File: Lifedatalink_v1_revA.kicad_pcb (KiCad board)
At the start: 4 copper layers, 69.5 x 72.5 mm, 88 parts, among them J1 DX07S024XJ1R1100, J10 503480-0400, J11 5034801400, J12 5034801400, J13 503480-0600, J14 503480-0600, J15 503480-0600, J16 503480-0600, J2 BATTERY CONNECTOR, J4 Conn_01x06, J5 503480-0400, J6 503480-0400, J7 503480-0400, J8 503480-0400, J9 503480-0400, Q1 DMG2301L, SW1 SW_Push, U1 BL654, U2 LP5907MFX-3_3_NOPB, U3 ADS1292R, U4 MCP73831-2-OT, U5 TMP117NAIYBGR, U6 MAX30102, U7 LP5907MFX-1.8, U8 IIS2DLPCTR, U9 PCA9306, Y1 Crystal

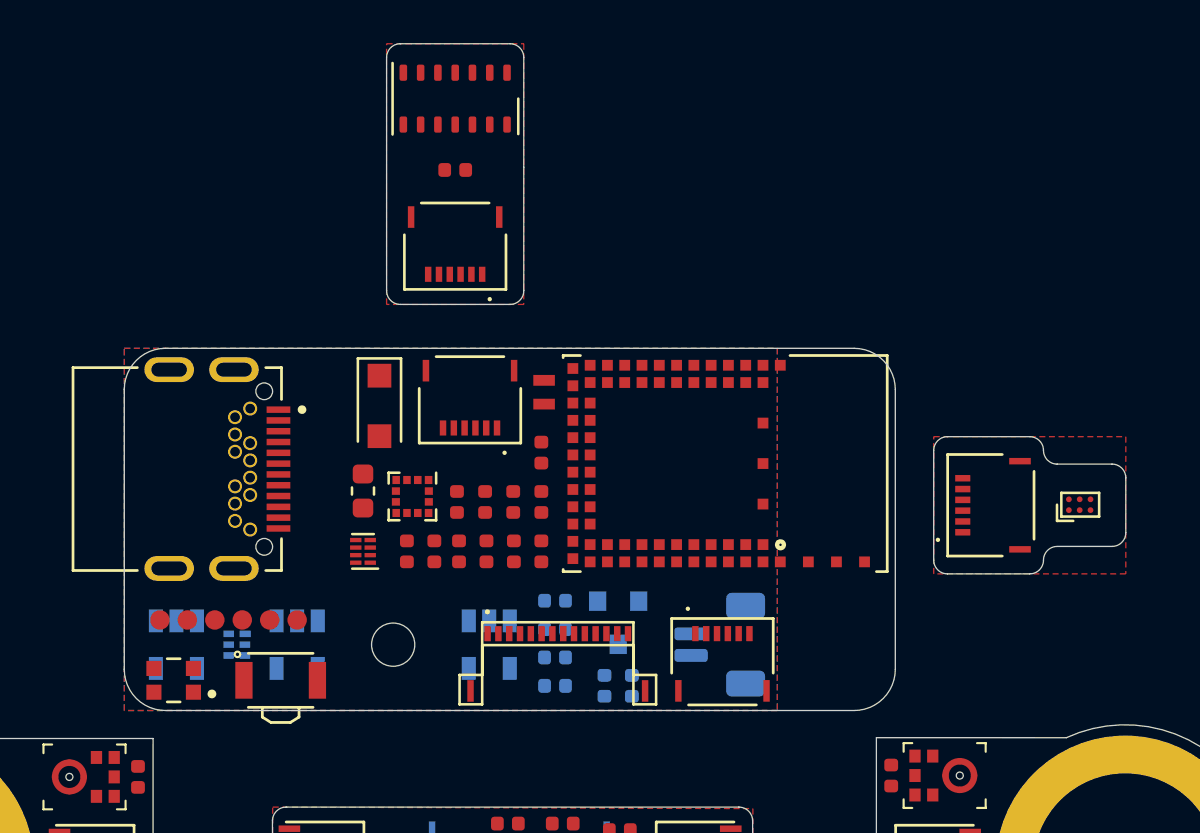
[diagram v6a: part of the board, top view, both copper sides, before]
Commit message: Main board routed
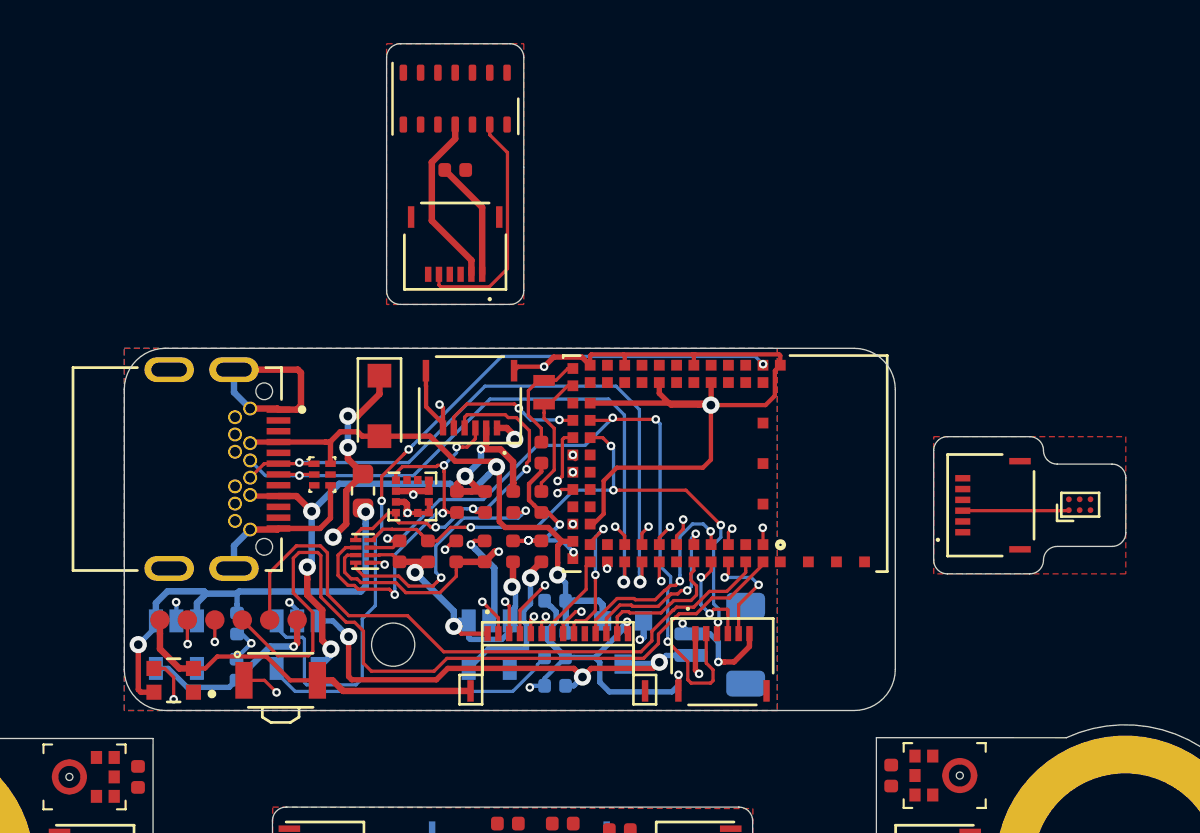
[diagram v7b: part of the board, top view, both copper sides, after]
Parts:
- D1: moved to F.Cu
- moved C3 18.5 mm to (73.1, 93.3)
- moved C4 14.9 mm to (73.1, 95.5), turned to 270 degrees
- moved D1 8.81 mm to (77.0, 86.4)
- moved R4 3.34 mm to (87.8, 93.8), turned to 0 degrees
- moved Q1 0.94 mm to (91.0, 94.2)
- moved R19 0.34 mm to (80.6, 90.0)
- moved R18 0.30 mm to (81.9, 90.0), turned to 90 degrees
- moved C28 0.13 mm to (83.2, 90.0)
- moved C27 0.09 mm to (84.5, 90.0)
- turned C25 to 270 degrees
- turned C26 to 270 degrees
- turned J4 to 180 degrees
- turned U8 to 0 degrees
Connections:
- C26 pad 1: Net-(C26-Pad1) -> GND
- C3 pad 2: Net-(C3-Pad2) -> /VIN
- D3 pad K: Net-(C3-Pad2) -> /VIN_FUSE
- F1 pad 1: Net-(F1-Pad1) -> /VIN
- F1 pad 2: Net-(C3-Pad2) -> /VIN_FUSE
- J11 pad 11: /BL654_I2S_WS -> /BL654_I2S_WS_EXT
- J11 pad 12: /BL654_I2S_SCK -> /BL654_I2S_SCK_EXT
- J11 pad 13: /BL654_I2S_SD -> /BL654_I2S_SD_EXT
- J11 pad 2: /ADS_SPI_SCLK -> /ADS_SPI_SCLK_EXT
- J11 pad 3: /ADS_SPI_MISO -> /ADS_SPI_MISO_EXT
- J11 pad 4: /ADS_SPI_MOSI -> /ADS_SPI_MOSI_EXT
- J11 pad 5: /~ADS_SPI_CS -> /~ADS_SPI_CS_EXT
- J11 pad 6: /~ADS_PWDN_RESET -> /~ADS_PWDN_RESET_EXT
- J11 pad 7: /ADS_START -> /ADS_START_EXT
- J11 pad 8: /ADS_CLK -> /ADS_CLK_EXT
- J11 pad 9: /~ADS_DRDY -> /~ADS_DRDY_EXT
- J13 pad 2: /BL654_I2C_SCL_HV -> /BL654_I2C_SCL_HV_EXT
- J13 pad 3: /BL654_I2C_SDA_HV -> /BL654_I2C_SDA_HV_EXT
- J13 pad 4: /TMP_ALERT -> /TMP_ALERT_EXT
- J13 pad 5: /TMP_ADD0 -> /TMP_ADD0_EXT
- J16 pad 3: /BL654_I2C_SCL_LV -> /BL654_I2C_SCL_LV_EXT
- J16 pad 4: /BL654_I2C_SDA_LV -> /BL654_I2C_SDA_LV_EXT
- J16 pad 5: /~MAX_INT -> /~MAX_INT_EXT
- J4 pad 1: Net-(J4-Pad1) -> +3V3
- MIC1 pad 1: /BL654_I2S_WS -> /BL654_I2S_WS_EXT
- MIC1 pad 4: /BL654_I2S_SCK -> /BL654_I2S_SCK_EXT
- MIC1 pad 6: /BL654_I2S_SD -> /BL654_I2S_SD_EXT
- MIC2 pad 1: /BL654_I2S_WS -> /BL654_I2S_WS_EXT
- MIC2 pad 4: /BL654_I2S_SCK -> /BL654_I2S_SCK_EXT
- MIC2 pad 6: /BL654_I2S_SD -> /BL654_I2S_SD_EXT
- Q1 pad 2: Net-(C3-Pad2) -> /VIN_FUSE
- R22 pad 1: /BL654_I2S_SD -> /BL654_I2S_SD_EXT
- U1 pad 12: Net-(U1-Pad12) -> /ADS_SPI_SCLK
- U1 pad 13: Net-(U1-Pad13) -> /ADS_SPI_MISO
- U1 pad 14: Net-(U1-Pad14) -> /ADS_SPI_MOSI
- U1 pad 16: Net-(U1-Pad16) -> /~ADS_PWDN_RESET
- U1 pad 18: Net-(U1-Pad18) -> /ADS_CLK
- U1 pad 19: Net-(U1-Pad19) -> /~ADS_SPI_CS
- U1 pad 21: Net-(U1-Pad21) -> /ADS_START
- U1 pad 22: Net-(U1-Pad22) -> /~ADS_DRDY
- U1 pad 30: /ADS_CLK -> Net-(U1-Pad30)
- U1 pad 32: /~ADS_DRDY -> Net-(U1-Pad32)
- U1 pad 37: Net-(U1-Pad37) -> /~MAX_INT
- U1 pad 44: /TMP_ADD0 -> Net-(U1-Pad44)
- U1 pad 5: Net-(U1-Pad5) -> /TMP_ADD0
- U1 pad 51: /ADS_SPI_MISO -> Net-(U1-Pad51)
- U1 pad 53: /ADS_SPI_SCLK -> Net-(U1-Pad53)
- U1 pad 54: /~ADS_SPI_CS -> Net-(U1-Pad54)
- U1 pad 56: /ADS_SPI_MOSI -> Net-(U1-Pad56)
- U1 pad 60: /~ADS_PWDN_RESET -> Net-(U1-Pad60)
- U1 pad 62: /ADS_START -> Net-(U1-Pad62)
- U2 pad 1: Net-(F1-Pad1) -> /VIN
- U2 pad 3: Net-(F1-Pad1) -> /VIN
- U3 pad 15: /~ADS_PWDN_RESET -> /~ADS_PWDN_RESET_EXT
- U3 pad 16: /ADS_START -> /ADS_START_EXT
- U3 pad 17: /ADS_CLK -> /ADS_CLK_EXT
- U3 pad 18: /~ADS_SPI_CS -> /~ADS_SPI_CS_EXT
- U3 pad 19: /ADS_SPI_MOSI -> /ADS_SPI_MOSI_EXT
- U3 pad 20: /ADS_SPI_SCLK -> /ADS_SPI_SCLK_EXT
- U3 pad 21: /ADS_SPI_MISO -> /ADS_SPI_MISO_EXT
- U3 pad 22: /~ADS_DRDY -> /~ADS_DRDY_EXT
- U5 pad A1: /BL654_I2C_SDA_HV -> /BL654_I2C_SDA_HV_EXT
- U5 pad A2: /BL654_I2C_SCL_HV -> /BL654_I2C_SCL_HV_EXT
- U5 pad C1: /TMP_ADD0 -> /TMP_ADD0_EXT
- U5 pad C2: /TMP_ALERT -> /TMP_ALERT_EXT
- U6 pad 13: /~MAX_INT -> /~MAX_INT_EXT
- U6 pad 2: /BL654_I2C_SCL_LV -> /BL654_I2C_SCL_LV_EXT
- U6 pad 3: /BL654_I2C_SDA_LV -> /BL654_I2C_SDA_LV_EXT
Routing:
- net GND: track 0.00 -> 121.3 mm, vias 0 -> 20
- net +3V3: track 0.00 -> 64.4 mm, vias 0 -> 8
- net +5V: track 0.00 -> 47.7 mm, vias 0 -> 5
- net +1V8: track 0.00 -> 45.7 mm, vias 0 -> 5
- net /WS2812_DATA: track 0.00 -> 38.5 mm, vias 0 -> 2
- net /BL654_SWDIO: track 0.00 -> 37.3 mm
- net /MCP73831_STAT: track 0.00 -> 36.5 mm, vias 0 -> 3
- net /BL654_I2C_SCL_HV: track 0.00 -> 34.3 mm, vias 0 -> 4
- net Net-(SW1-Pad1): track 0.00 -> 31.4 mm, vias 0 -> 2
- net /BL654_SWDCLK: track 0.00 -> 30.2 mm
- net /BL654_USB_DP: track 0.00 -> 29.9 mm, vias 0 -> 2
- net /BL654_USB_DN: track 0.00 -> 29.7 mm, vias 0 -> 2
- net /BL654_UART_RX: track 0.00 -> 28.5 mm, vias 0 -> 2
- net /BL654_UART_TX: track 0.00 -> 27.5 mm, vias 0 -> 2
- net /VIN_FUSE: track 0.00 -> 27.4 mm, vias 0 -> 4
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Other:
- net class Power: clearance 0.2 -> 0.1524

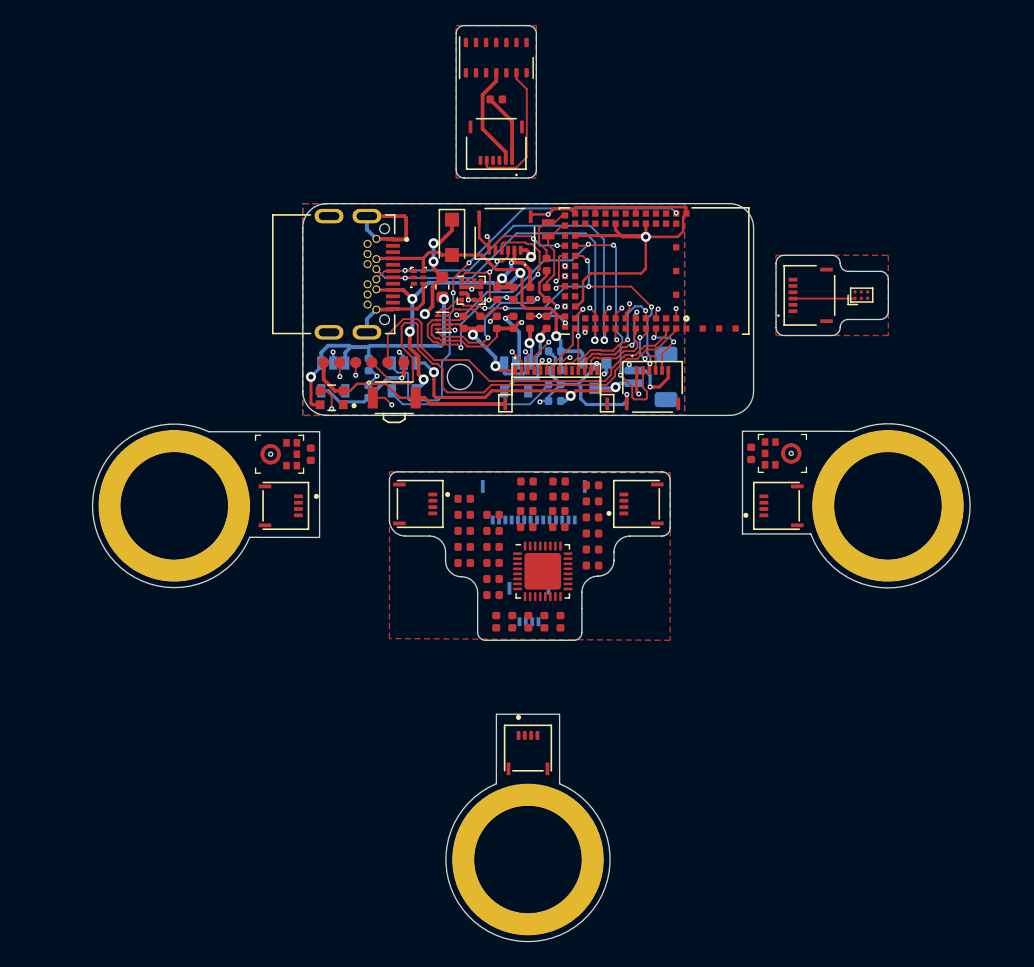
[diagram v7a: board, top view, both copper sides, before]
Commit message: Completed routing of all boards
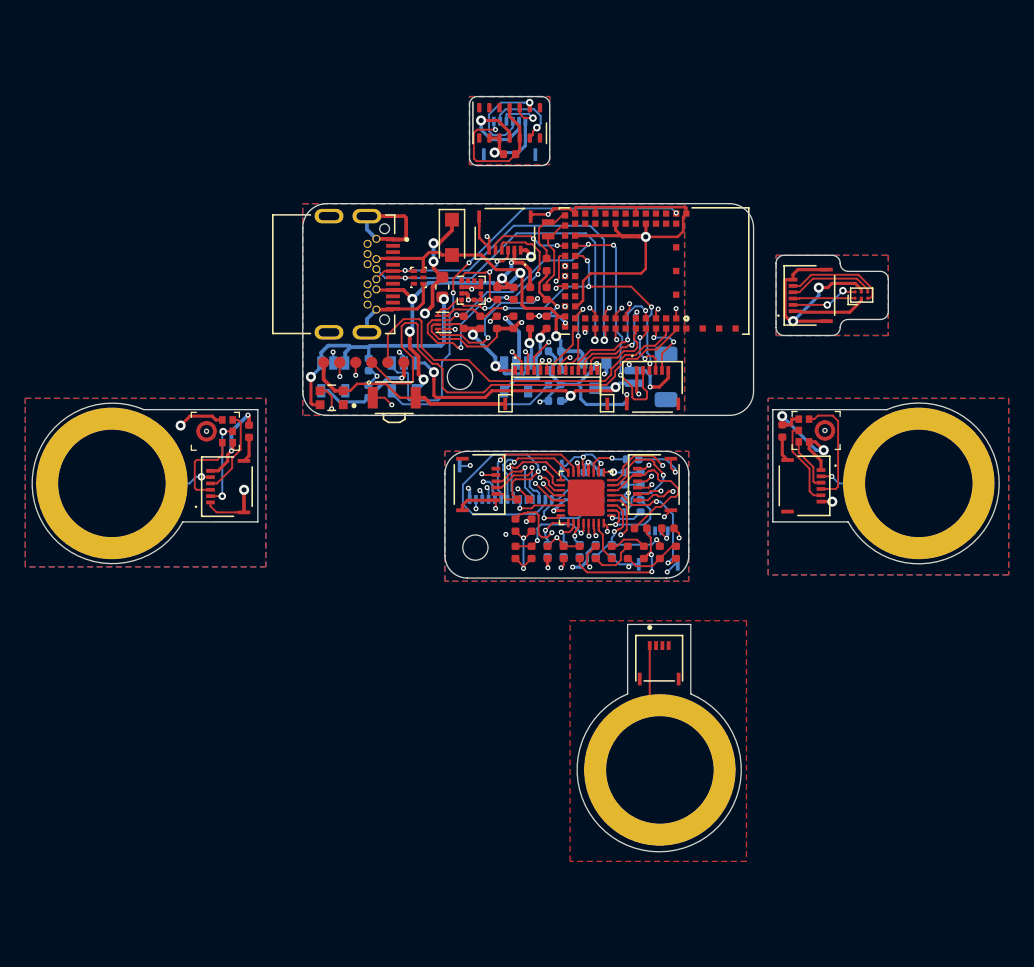
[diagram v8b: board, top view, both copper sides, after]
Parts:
- removed the REF** at (85.7, 132.5)
- removed the REF** at (57.7, 104.5)
- removed the REF** at (114.2, 104.5)
- added J17: 503480-0600, MOLEX_503480-0600:MOLEX_503480-0600, F.Cu at (62.0, 103.0)
- added J18: ECG_RIGHT_LEG, MOLEX_503480-0600:ECG_SNAP, F.Cu at (96.1, 125.4)
- added J3: 503480-0600, MOLEX_503480-0600:MOLEX_503480-0600, F.Cu at (95.8, 102.8)
- added P6: HORIZON MEDICAL LOGO, horizon_logo_silk:horizon_logo_silk, B.Cu at (86.4, 86.1)
- added REF**: MountingHole_2mm, MountingHole:MountingHole_2mm, B.Cu at (81.5, 107.8)
- C10, C11, C12, C13, C14, C22, C23, C5, C8, C9, J16, R10, R15, R16, R9: moved to B.Cu
- J5, J8: value 503480-0400 -> 503480-0600; footprint 503480-0400:MOLEX_503480-0400 -> MOLEX_503480-0600:MOLEX_503480-0600
- J6: value 503480-0400 -> ECG_LEFT_ARM; footprint 503480-0400:MOLEX_503480-0400 -> MOLEX_503480-0600:ECG_SNAP
- J7: value 503480-0400 -> ECG_RIGHT_ARM; footprint 503480-0400:MOLEX_503480-0400 -> MOLEX_503480-0600:ECG_SNAP
- moved J7 24.1 mm to (52.8, 102.7), turned to 0 degrees
- moved J8 15.7 mm to (81.8, 102.8)
- moved C11 15.3 mm to (94.0, 100.8), turned to 180 degrees
- moved C10 15.2 mm to (94.6, 102.4)
- moved C9 15.2 mm to (93.3, 102.4)
- moved C17 14.2 mm to (94.6, 106.3), turned to 180 degrees
- moved C16 14.2 mm to (94.9, 108.2), turned to 270 degrees
- moved C13 13.0 mm to (94.6, 104.5), turned to 270 degrees
- moved J5 13.0 mm to (107.5, 102.9), turned to 270 degrees
- moved J10 12.6 mm to (96.1, 116.9)
- moved C14 12.6 mm to (93.3, 104.5), turned to 270 degrees
- moved C5 11.8 mm to (90.2, 102.4)
- moved C8 11.8 mm to (91.4, 102.4)
- moved R14 11.8 mm to (96.8, 106.3)
- moved J9 11.2 mm to (96.0, 107.8), turned to 180 degrees
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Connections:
- net RIGHT_LEG renamed /ECG_RIGHT_LEG
- C17 pad 2: LEFT_ARM -> /ECG_LEFT_ARM
- C19 pad 2: RIGHT_ARM -> /ECG_RIGHT_ARM
- J10 pad S1: Net-(J10-PadS1) -> GND
- J10 pad S2: Net-(J10-PadS1) -> GND
- J5 pad 1: LEFT_ARM -> +3V3
- J5 pad 2: Net-(J5-Pad2) -> /ECG_LEFT_ARM
- J5 pad 3: Net-(J5-Pad3) -> /BL654_I2S_WS_EXT
- J5 pad 4: Net-(J5-Pad4) -> /BL654_I2S_SCK_EXT
- J5 pad S1: Net-(J5-PadS1) -> GND
- J5 pad S2: Net-(J5-PadS1) -> GND
- J6 pad 1: LEFT_ARM -> /ECG_LEFT_ARM
- J7 pad 1: RIGHT_ARM -> /ECG_RIGHT_ARM
- J8 pad 1: RIGHT_ARM -> Net-(J8-Pad1)
- J8 pad 2: Net-(J8-Pad2) -> /ECG_RIGHT_ARM
- J8 pad 3: Net-(J8-Pad3) -> /BL654_I2S_WS_EXT
- J8 pad 4: Net-(J8-Pad4) -> /BL654_I2S_SCK_EXT
- J8 pad S1: Net-(J8-PadS1) -> GND
- J8 pad S2: Net-(J8-PadS1) -> GND
- J9 pad S1: Net-(J9-PadS1) -> GND
- J9 pad S2: Net-(J9-PadS1) -> GND
- U3 pad 5: RIGHT_ARM -> /ECG_RIGHT_ARM
- U3 pad 6: LEFT_ARM -> /ECG_LEFT_ARM
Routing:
- net GND: track 121.3 -> 242.4 mm, vias 20 -> 38
- net +3V3: track 64.4 -> 130.8 mm, vias 8 -> 21
- net /BL654_I2S_SD_EXT: track 0.00 -> 49.4 mm, vias 0 -> 4
- net /ECG_RIGHT_ARM: track 0.00 -> 34.6 mm, vias 0 -> 4
- net /BL654_I2S_SCK_EXT: track 0.00 -> 34.3 mm, vias 0 -> 2
- net /BL654_I2S_WS_EXT: track 0.00 -> 29.2 mm, vias 0 -> 2
- net Net-(C21-Pad2): track 0.00 -> 19.8 mm, vias 0 -> 3
- net /ECG_LEFT_ARM: track 0.00 -> 19.8 mm, vias 0 -> 1
- net Net-(C15-Pad2): track 0.00 -> 12.5 mm, vias 0 -> 2
- net /ECG_RIGHT_LEG: track 0.00 -> 11.7 mm, vias 0 -> 1
- net Net-(C15-Pad1): track 0.00 -> 11.3 mm, vias 0 -> 2
- net Net-(C14-Pad2): track 0.00 -> 10.8 mm, vias 0 -> 1
- net Net-(C20-Pad2): track 0.00 -> 10.3 mm, vias 0 -> 2
- net /RLDOUT: track 0.00 -> 10.2 mm, vias 0 -> 2
- net /~ADS_PWDN_RESET_EXT: track 0.00 -> 10.1 mm, vias 0 -> 1
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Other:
- board size 69.5 x 72.5 mm -> 76.6 x 59.8 mm
- board text added: "LifeDataLinkv1RevA"
